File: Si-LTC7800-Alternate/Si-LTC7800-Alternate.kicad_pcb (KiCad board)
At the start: 2 copper layers, 92.2 x 47.8 mm, 40 parts, among them Q1 BSC100N06LS3_G, Q2 BSC100N06LS3_G, U1 LTC7800HUDC_PBF

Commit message: Updating PCBs for preassembly
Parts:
- added RLOAD2: 2Ohm, Resistor_SMD:R_0201_0603Metric, F.Cu at (153.0, 125.7)
- C1, C2, C3, C5, C6, COUT1, CSENSE1, CinA1, CinA2: footprint Capacitor_SMD:C_0805_2012Metric_Pad1.18x1.45mm_HandSolder -> Capacitor_SMD:C_0805_2012Metric
- CinB1: footprint Capacitor_SMD:C_0805_2012Metric_Pad1.18x1.45mm_HandSolder -> Capacitor_Tantalum_SMD:CP_EIA-7343-31_Kemet-D
- R1, R2, R4, R5, R6, R7, R9, RSENSE1: footprint Resistor_SMD:R_0201_0603Metric_Pad0.64x0.40mm_HandSolder -> Resistor_SMD:R_0201_0603Metric
- RLOAD1: value 5Ohm -> 3Ohm; footprint Resistor_SMD:R_0201_0603Metric_Pad0.64x0.40mm_HandSolder -> Resistor_SMD:R_0201_0603Metric
- moved CinB1 27.5 mm to (161.2, 156.4), turned to 90 degrees
- moved RLOAD1 6.06 mm to (154.2, 127.0), turned to 135 degrees
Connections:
- RLOAD1 pad 2: GND -> Net-(RLOAD1-Pad2)
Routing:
- net /VIN: track 105.4 -> 97.9 mm
- net Net-(RLOAD1-Pad2): track 0.00 -> 1.17 mm

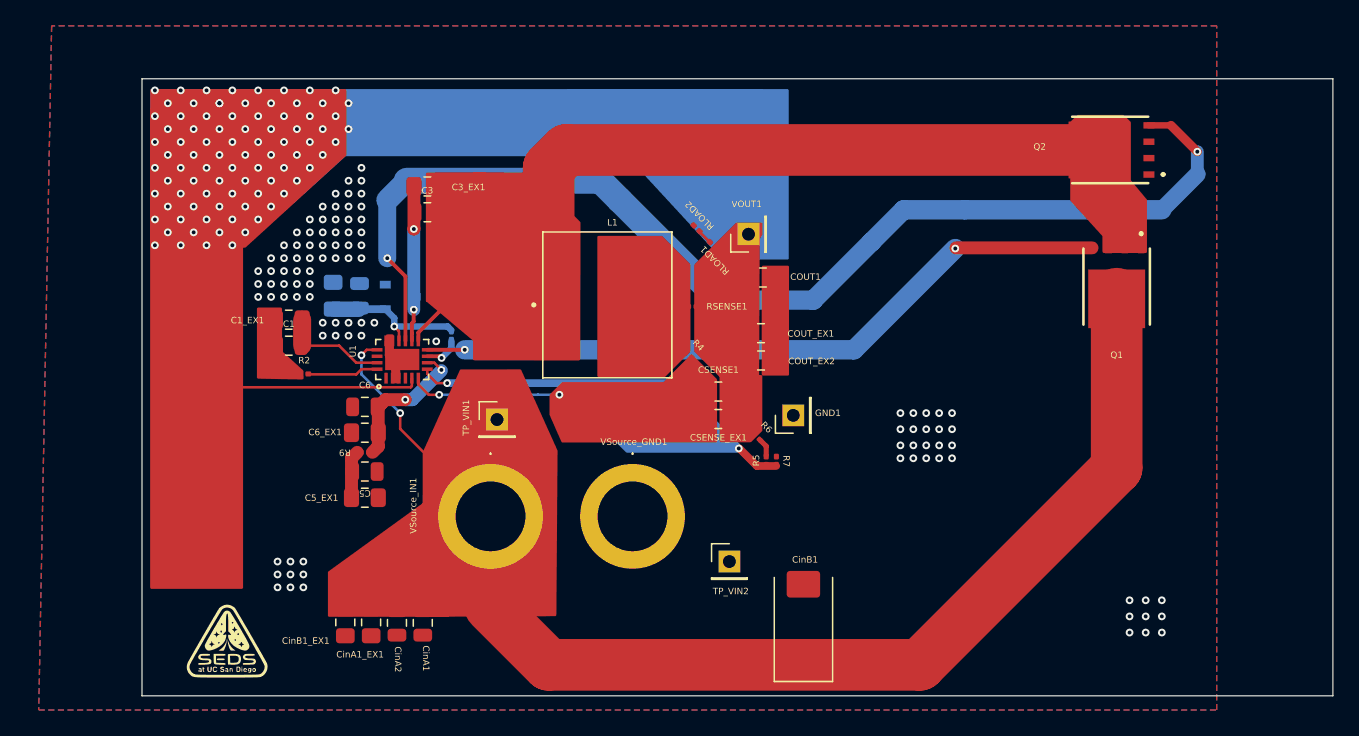
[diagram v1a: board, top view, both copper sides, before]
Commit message: mounting holes
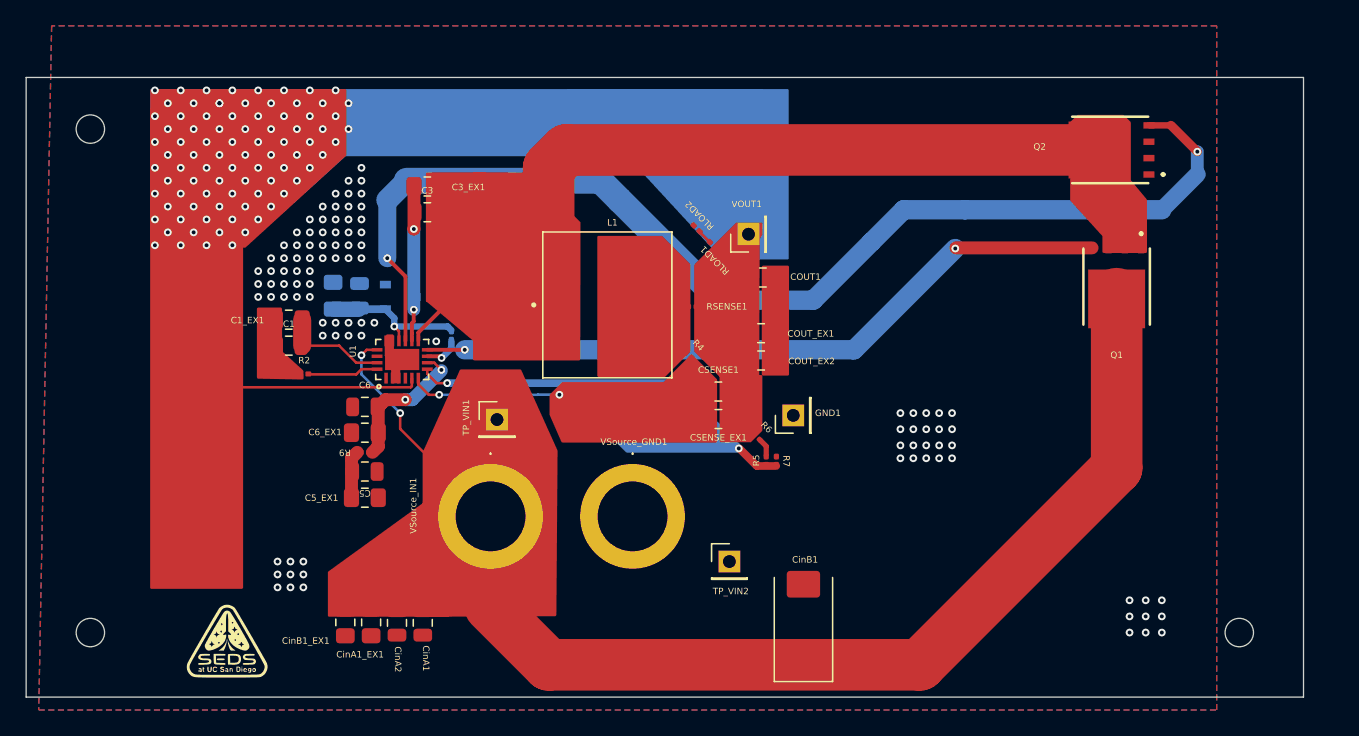
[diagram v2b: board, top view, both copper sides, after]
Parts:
- added REF**: MountingHole_2.2mm_M2, MountingHole:MountingHole_2.2mm_M2, F.Cu at (106.0, 157.0)
- added REF**: MountingHole_2.2mm_M2, MountingHole:MountingHole_2.2mm_M2, F.Cu at (106.0, 118.0)
- added REF**: MountingHole_2.2mm_M2, MountingHole:MountingHole_2.2mm_M2, F.Cu at (195.0, 157.0)
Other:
- board size 92.2 x 47.8 mm -> 98.9 x 48 mm

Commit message: minor edits
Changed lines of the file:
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@@
 		(polygon
 			(pts
-				(xy 103 110) (xy 102 163) (xy 193.25 163) (xy 193.25 110)
+				(xy 101.053284 114.002365) (xy 101.053284 162.019286) (xy 200.158944 161.90274) (xy 199.909203 113.877494)
 			)
 		)
